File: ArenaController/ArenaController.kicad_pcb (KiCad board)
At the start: 2 copper layers, 80 x 90 mm, 29 parts, among them J1 RJ45, J2 RJ45, J4 RJ45, J5 RJ45, J6 RJ45, J9 Barrel_Jack_MountingPin, Q1 FS3400, Q2 FS3400, Q3 FS3400, Q4 FS3400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

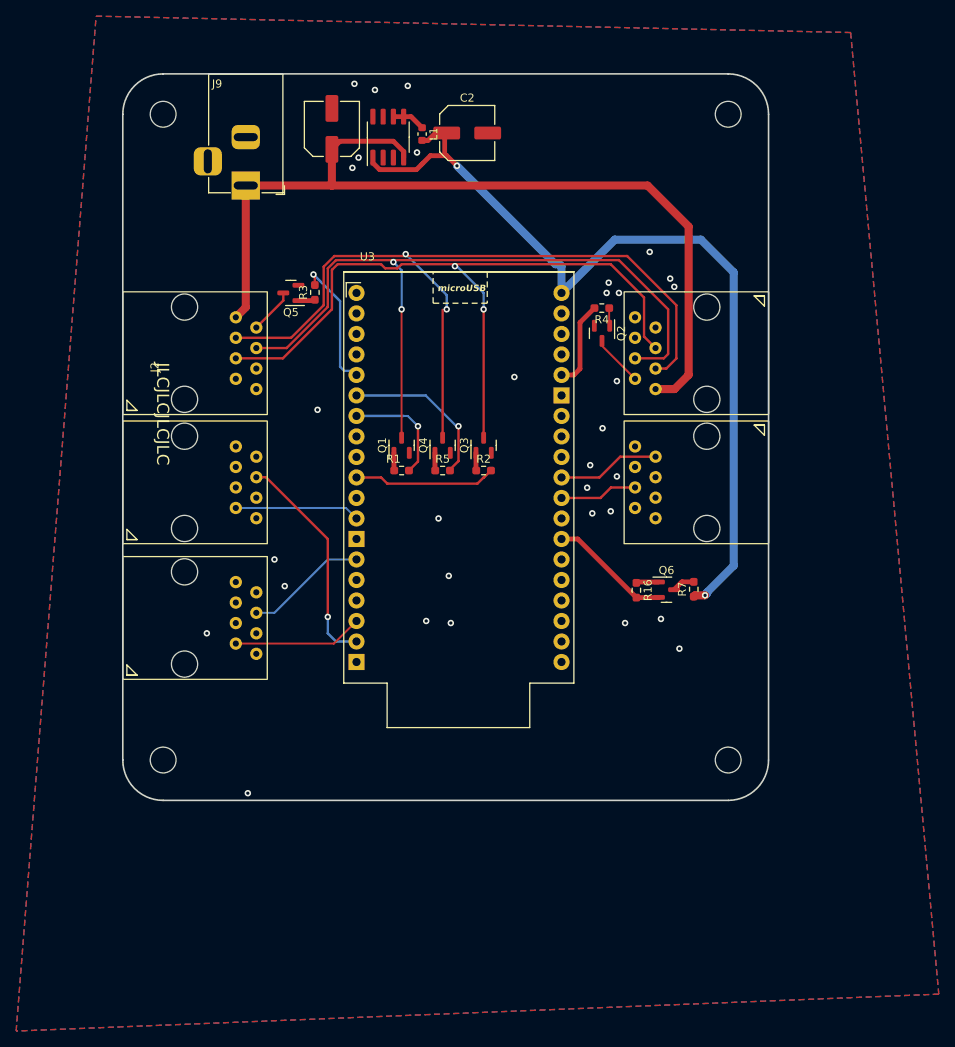
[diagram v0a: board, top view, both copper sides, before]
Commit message: Update fp to include fixed keepouts for the THT part module.
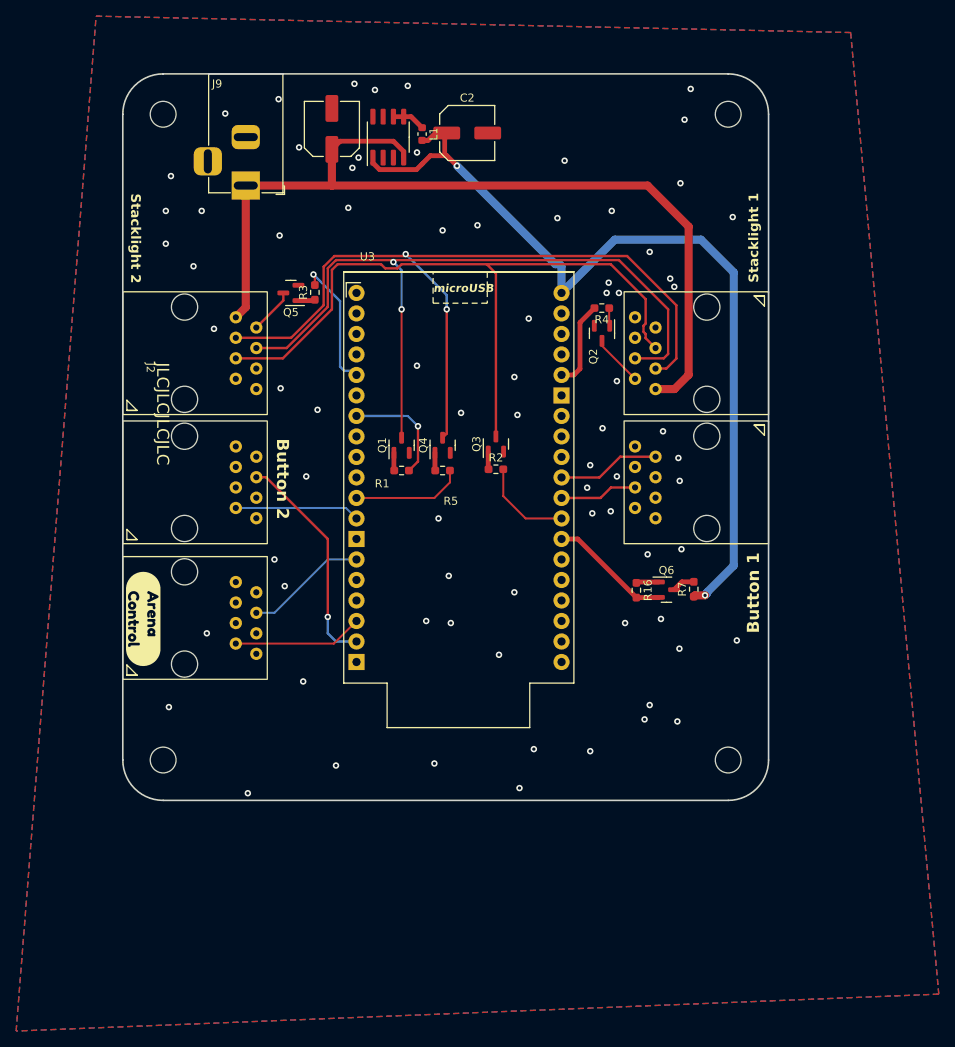
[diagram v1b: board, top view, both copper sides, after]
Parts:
- kibuzzard-638A219C: moved to F.Cu
- moved Q3 1.53 mm to (141.2, 90.9)
- moved R2 1.53 mm to (141.2, 94.0)
- moved kibuzzard-638A219C 0.36 mm to (97.5, 112.5), turned to -90 degrees
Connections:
- U3 pad 10: /m_Horn -> unconnected-(U3-GPIO5/V_SPI_CS0/SS-Pad10)
- U3 pad 11: unconnected-(U3-GPIO18/V_SPI_CLK/SCK-Pad11) -> /m_Yellow
- U3 pad 27: unconnected-(U3-RTC_GPIO8/Xtal32N/Touch8/ADC1_5/GPIO33-Pad27) -> /m_Horn
- U3 pad 6: /m_Yellow -> unconnected-(U3-GPIO0/ADC2_1/CLK1/Touch1/RTC_GPIO11-Pad6)
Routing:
- net /m_Yellow: track 19.9 -> 13.8 mm, vias 1 -> 0
- net /m_Horn: track 17.6 -> 11.7 mm
- net /s_Horn: track 90.1 -> 89.3 mm, vias 2 -> 0
- net GND: vias 32 -> 76

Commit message: Add SK6812-Side-A footprint/symbol to working area, as well as swapped to a stacklight connection that has a ground pin at the end for generic 12v power use.  yay!
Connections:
- J1 pad 8: unconnected-(J1-Pad8) -> GND
- J2 pad 8: unconnected-(J2-Pad8) -> GND

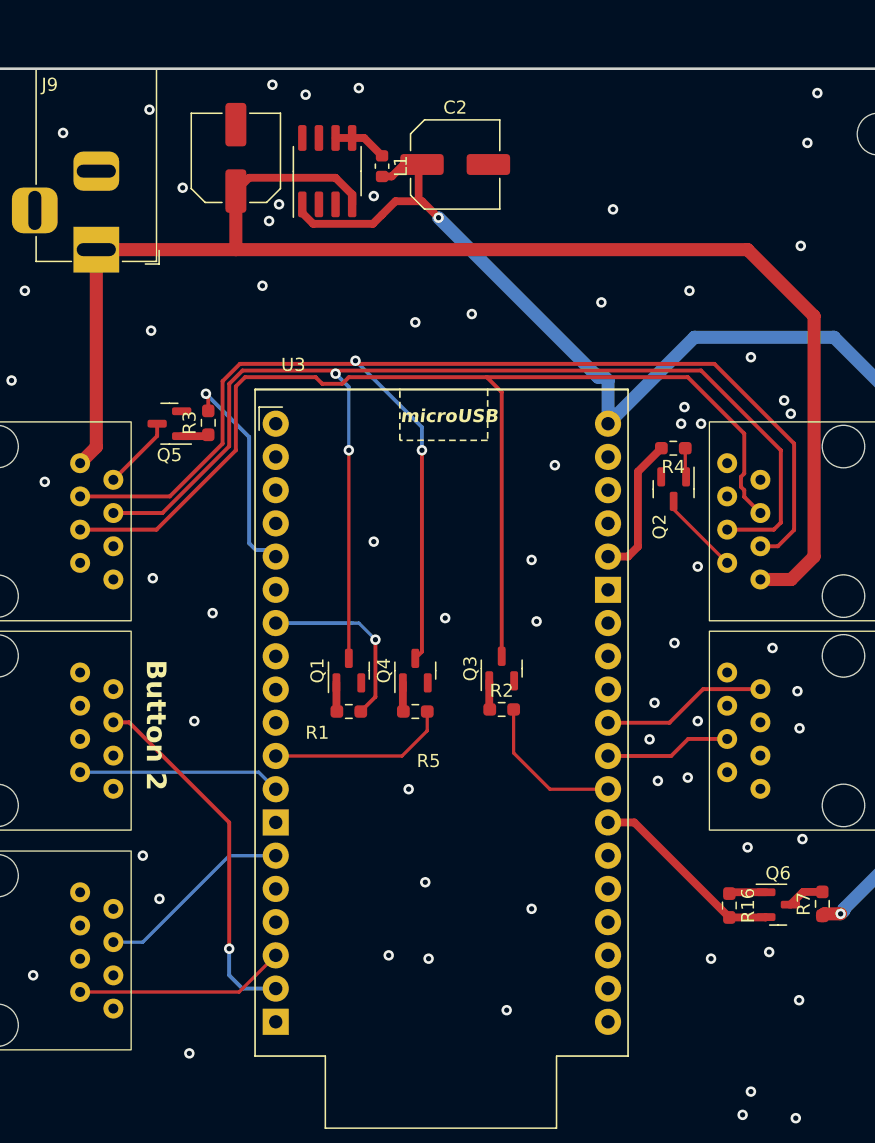
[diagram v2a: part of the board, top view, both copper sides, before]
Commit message: Added reset pins back in and broke out the pins in the team control area; should be easier now.  Yay!
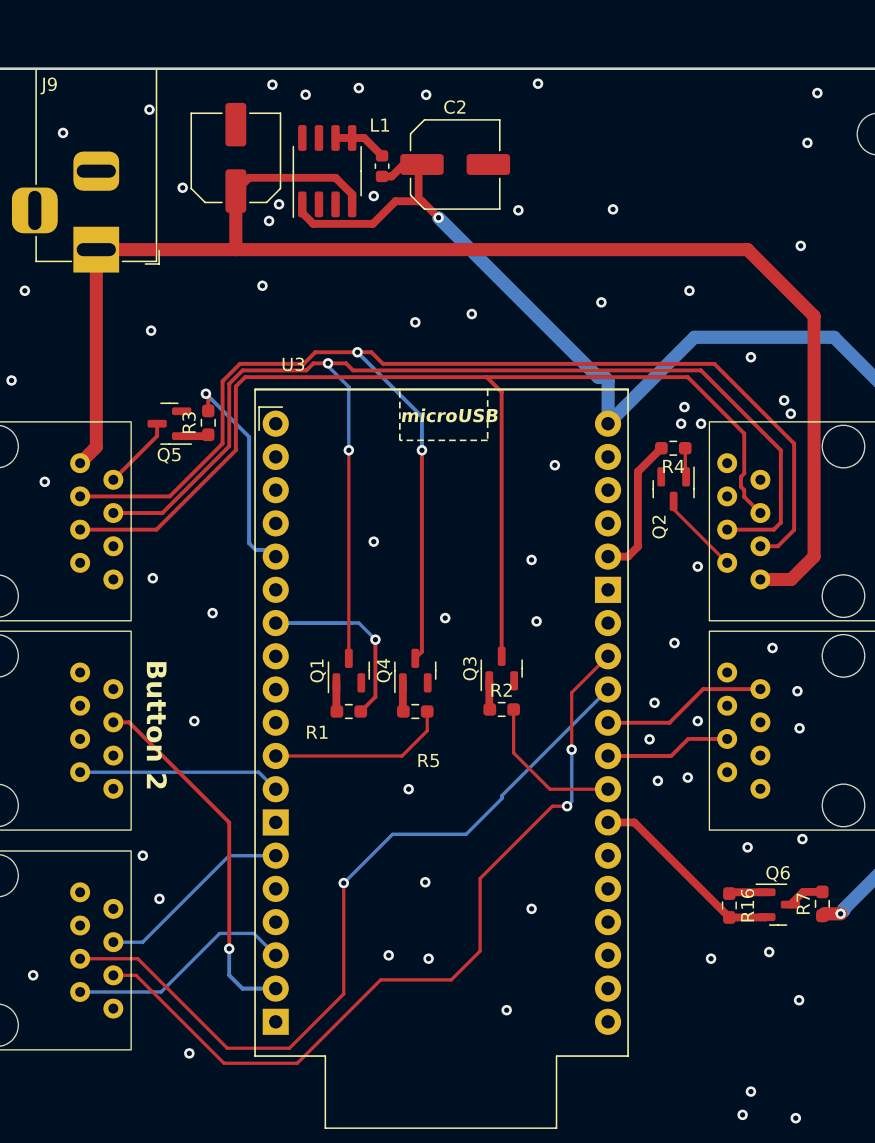
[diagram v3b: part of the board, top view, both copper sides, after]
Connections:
- J4 pad 5: unconnected-(J4-Pad5) -> /G_RST
- J4 pad 6: unconnected-(J4-Pad6) -> /G_Pause
- U3 pad 30: unconnected-(U3-RTC_GPIO17/Touch7/ADC2_7/GPIO27-Pad30) -> /G_RST
- U3 pad 31: unconnected-(U3-RTC_GPIO16/Touch6/HSPI_CLK/ADC2_6/GPIO14-Pad31) -> /G_Pause
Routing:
- net /G_Pause: track 0.00 -> 61.6 mm, vias 0 -> 2
- net /G_RST: track 0.00 -> 59.6 mm, vias 0 -> 1
- net /s_Green: track 92.9 -> 94.4 mm
- net /G_End: track 16.1 -> 17.5 mm
- net /s_Yellow: track 98.9 -> 100.2 mm
- net GND: vias 76 -> 79
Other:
- board text added: "Arena Controller v0.5 Kim Chase & Neil Flynn"
- board text removed: "Arena Controller v.4 Kim Chase & Neil Flynn"

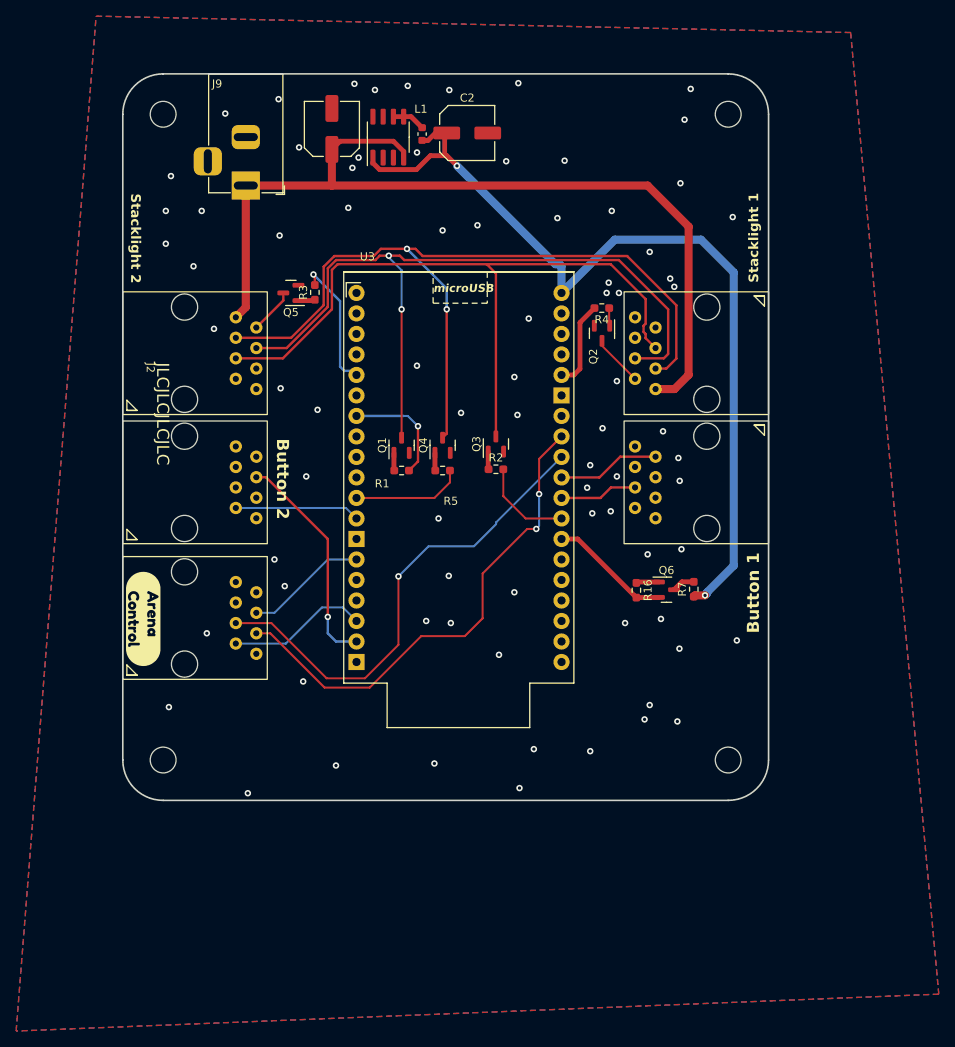
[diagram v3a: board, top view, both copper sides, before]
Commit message: Add new inductor, add new chip resistor.
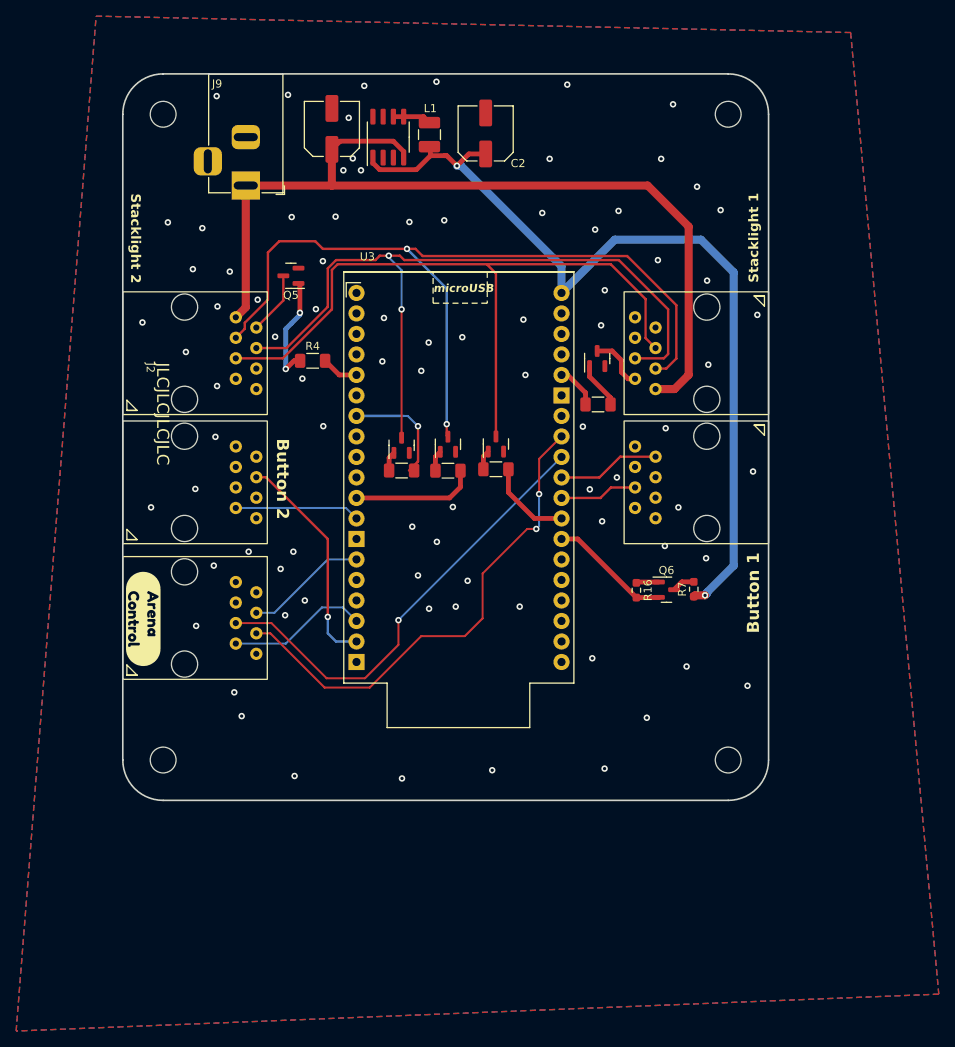
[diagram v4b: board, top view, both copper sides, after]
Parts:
- L1: footprint Inductor_SMD:L_0603_1608Metric -> Inductor_SMD:L_1210_3225Metric_Pad1.42x2.65mm_HandSolder
- R1, R2, R3, R4, R5: footprint Resistor_SMD:R_0603_1608Metric_Pad0.98x0.95mm_HandSolder -> Resistor_SMD:R_1206_3216Metric_Pad1.30x1.75mm_HandSolder
- moved R4 36.4 mm to (118.5, 80.5), turned to 0 degrees
- moved R3 27.6 mm to (135.3, 94.2), turned to 0 degrees
- moved R5 20.9 mm to (153.9, 86.0), turned to 180 degrees
- moved Q2 3.18 mm to (153.8, 80.3), turned to 90 degrees
- moved C2 2.29 mm to (140.0, 52.4), turned to 90 degrees
- moved Q5 2.12 mm to (115.8, 70.0)
- moved L1 0.92 mm to (133.0, 52.5)
- moved Q4 0.67 mm to (135.3, 90.9)
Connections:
- R3 pad 1: Net-(Q5-G) -> Net-(Q4-G)
- R3 pad 2: /m_Red_2 -> /m_Yellow
- R4 pad 1: Net-(Q2-G) -> Net-(Q5-G)
- R4 pad 2: /m_Red_1 -> /m_Red_2
- R5 pad 1: Net-(Q4-G) -> Net-(Q2-G)
- R5 pad 2: /m_Yellow -> /m_Red_1
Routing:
- net Net-(Q5-G): track 1.93 -> 13.6 mm, vias 0 -> 2
- net /m_Red_2: track 15.9 -> 4.61 mm, vias 1 -> 0
- net /m_Red_1: track 10.9 -> 5.33 mm
- net Net-(Q2-G): track 2.13 -> 5.83 mm
- net /G_RST: track 59.6 -> 56.3 mm
- net /s_Red_2: track 5.68 -> 7.80 mm
- net /m_Yellow: track 13.8 -> 15.5 mm
- net /s_Yellow: track 100.2 -> 101.7 mm
- net /s_Red_1: track 5.79 -> 6.98 mm
- net /m_Horn: track 11.7 -> 10.8 mm
- net Net-(L1-Pad1): track 4.12 -> 4.78 mm
- net +5V: track 108.1 -> 107.4 mm
- net GND: vias 79 -> 85
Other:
- board text added: "Arena Controller v0.6 Kim Chase & Neil Flynn"
- board text removed: "Arena Controller v0.5 Kim Chase & Neil Flynn"

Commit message: Update ArenaController footprints to be over the edge and line up with the printed enclosure.
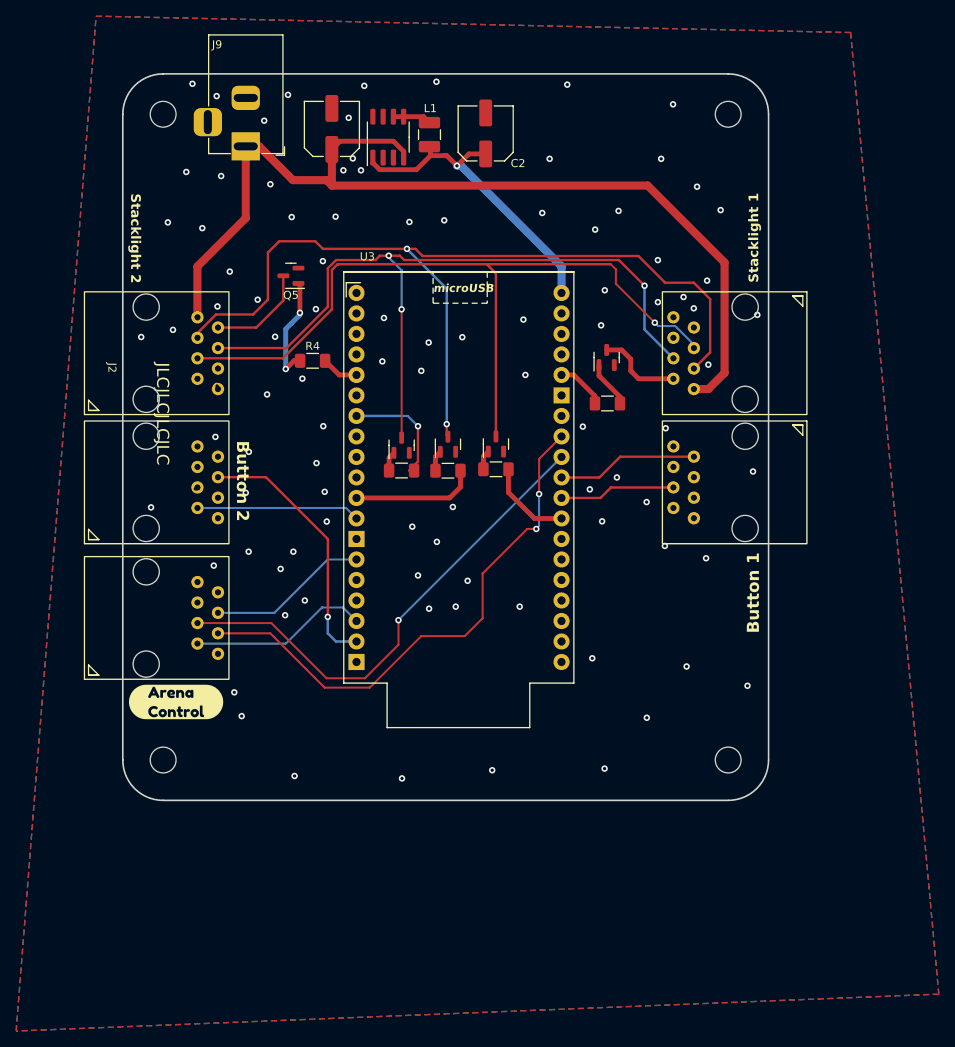
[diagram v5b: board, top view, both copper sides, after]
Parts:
- removed Q6: Q_NMOS_GSD, Package_TO_SOT_SMD:SOT-23
- removed R16, R7: 10k, Resistor_SMD:R_0603_1608Metric_Pad0.98x0.95mm_HandSolder
- moved kibuzzard-638A219C 11.1 mm to (101.6, 122.8), turned to 0 degrees
- moved J9 4.86 mm to (110.2, 54.0)
- moved J1 4.75 mm to (179.8, 72.0)
- moved J2 4.75 mm to (90.2, 87.2)
- moved J4 4.75 mm to (90.2, 120.0)
- moved J5 4.75 mm to (90.2, 103.2)
- moved J6 4.75 mm to (179.8, 88.0)
- moved Q2 1.18 mm to (154.9, 80.1)
- moved R5 1.18 mm to (155.0, 85.8)
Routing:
- net +5V: track 107.4 -> 38.7 mm, vias 2 -> 1
- net /status_LED: track 15.1 -> 0.00 mm
- net +12V: track 112.1 -> 122.3 mm
- net /s_Yellow: track 101.7 -> 110.0 mm
- net /s_Horn: track 88.6 -> 96.6 mm, vias 0 -> 1
- net /T_B_Start: track 15.5 -> 20.2 mm
- net /T_A_Start: track 9.65 -> 14.4 mm
- net /T_A_End: track 12.7 -> 17.5 mm
- net /G_Start: track 15.1 -> 19.9 mm
- net /G_Pause: track 61.6 -> 66.4 mm
- net /G_End: track 17.5 -> 22.2 mm
- net /s_Red_2: track 7.80 -> 12.5 mm
- net /T_B_End: track 27.7 -> 32.4 mm
- net /G_RST: track 56.3 -> 60.9 mm
- net /s_Red_1: track 6.98 -> 10.6 mm
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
